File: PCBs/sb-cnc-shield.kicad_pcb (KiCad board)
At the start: 2 copper layers, 68.6 x 53.3 mm, 62 parts, among them P1 XMOT, P2 YMOT, P3 ZMOT, P4 AMOT, P5 UART, P6 I2C, P7 E-STOP, P8 12V-36V, SW1 RESET, U1 ARDUINO_UNO_SHIELD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

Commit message: modify name PCBs
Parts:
- P7: value E-STOP -> ES_SETUP

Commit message: add _SDC_ _SCL_ for hi five rev b board
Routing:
- net SPIN_DIR: track 142.8 -> 144.5 mm

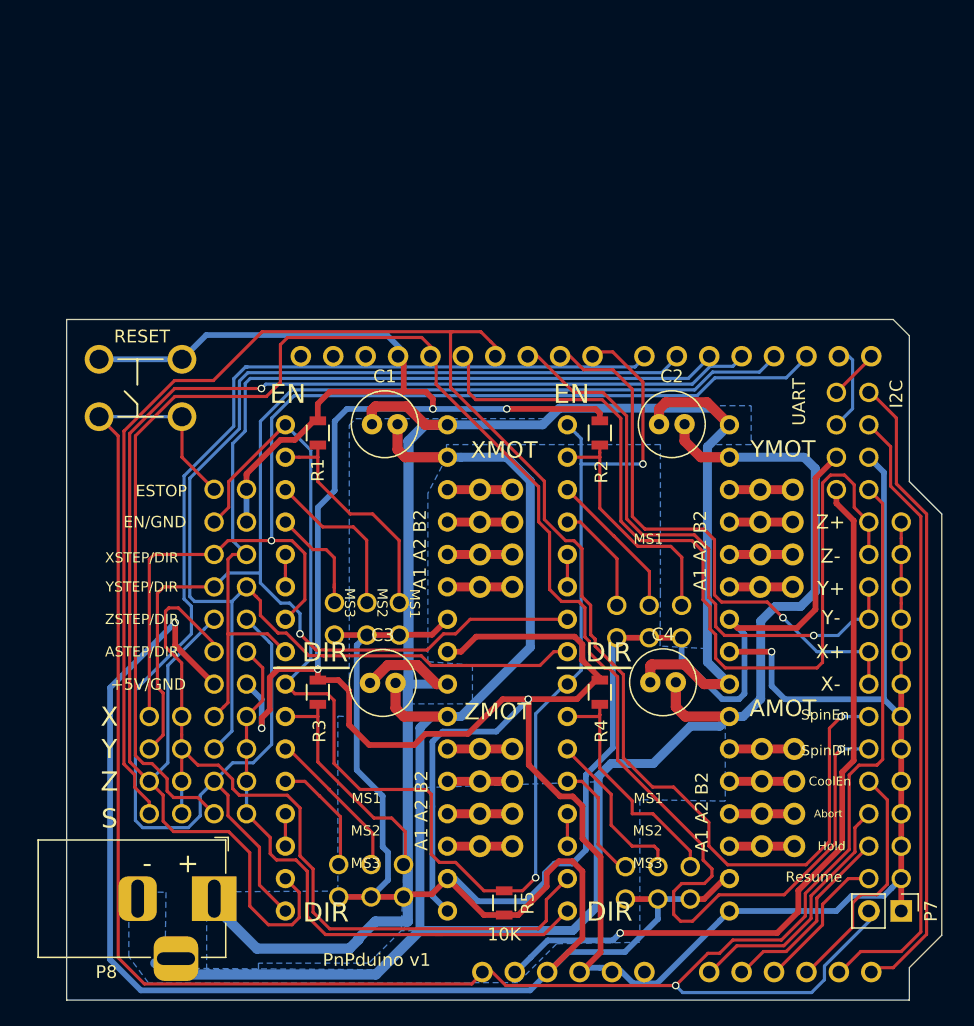
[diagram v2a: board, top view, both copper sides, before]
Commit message: add power button, lenghten pcb
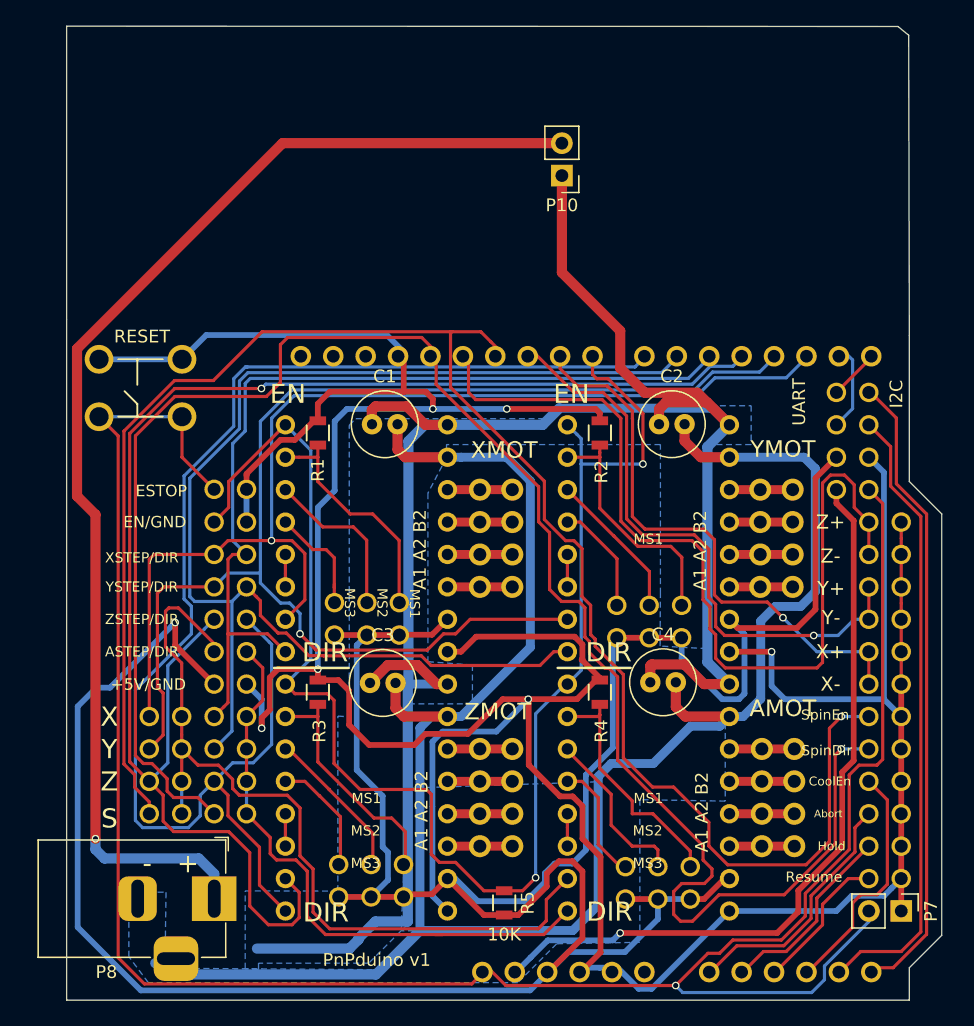
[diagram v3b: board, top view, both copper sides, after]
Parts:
- added P10: power switch, Connector_PinHeader_2.54mm:PinHeader_1x02_P2.54mm_Vertical, F.Cu at (153.1, 54.8)
- P7: value ES_SETUP -> E_STOP
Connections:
- P8 pad 1: VIN -> VIN_
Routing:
- net VIN_: track 0.00 -> 96.6 mm, vias 0 -> 1
- net VIN: track 139.2 -> 161.5 mm
- net +5V: track 226.4 -> 229.1 mm
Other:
- board size 68.6 x 53.3 mm -> 68.6 x 76.3 mm

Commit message: add pump management circuit, I2C JST conn for display, JST power switch
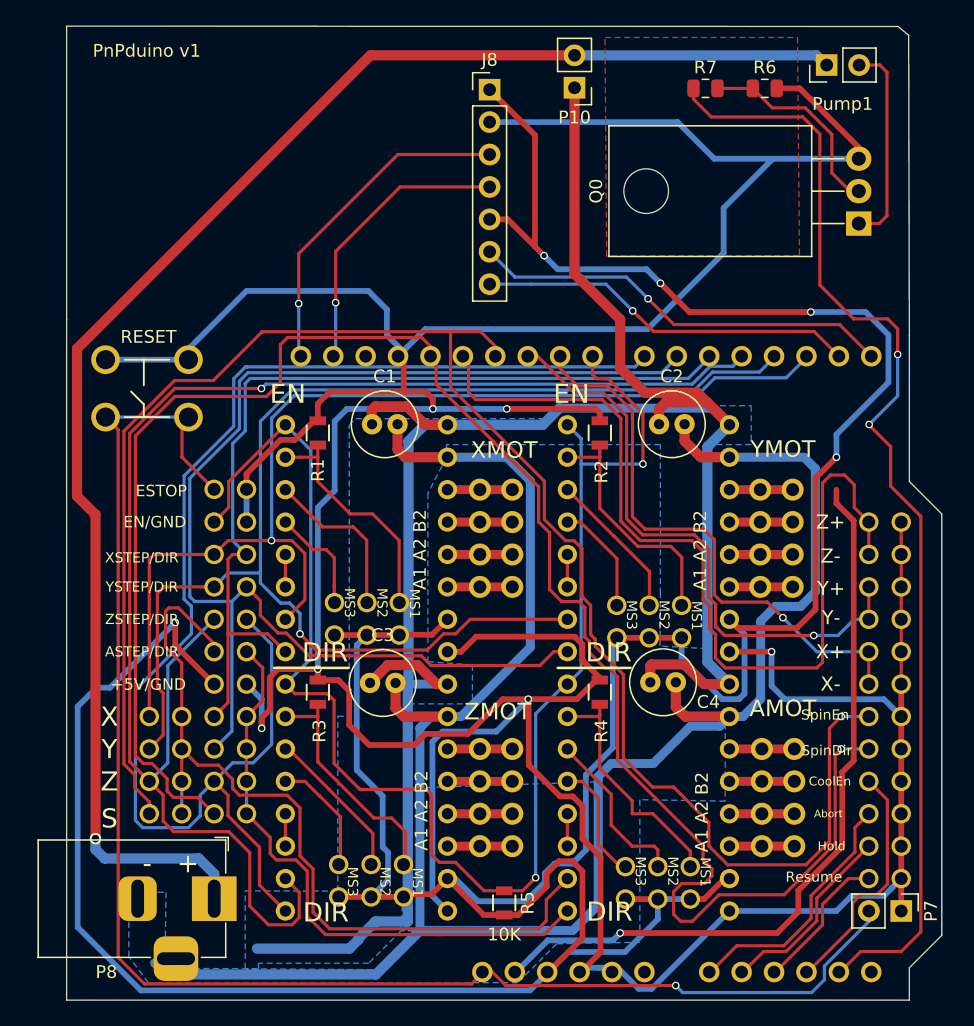
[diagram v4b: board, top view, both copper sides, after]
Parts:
- removed P5: UART, Pin_Headers:Pin_Header_Straight_1x04
- removed P6: I2C, Pin_Headers:Pin_Header_Straight_1x04
- added J8: display, Connector_PinHeader_2.54mm:PinHeader_1x07_P2.54mm_Vertical, F.Cu at (147.4, 48.0)
- added Pump1: pump, Connector_PinHeader_2.54mm:PinHeader_1x02_P2.54mm_Vertical, F.Cu at (173.9, 46.1)
- added Q0: IRF630, Package_TO_SOT_THT:TO-220-3_Horizontal_TabDown, F.Cu at (176.4, 58.5)
- added R6: 10K, Resistor_SMD:R_0805_2012Metric, F.Cu at (169.0, 47.9)
- added R7: 1K, Resistor_SMD:R_0805_2012Metric, F.Cu at (164.4, 47.9)
- moved P10 6.95 mm to (154.1, 47.9)
- moved SW1 0.51 mm to (117.3, 73.7)
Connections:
- U1 pad 1: RX -> DC
- U1 pad 2: TX -> res
- U1 pad 29: Net-(U1-Pad29) -> _SDA_
- U1 pad 30: Net-(U1-Pad30) -> _SCL_
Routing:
- net GND: track 292.6 -> 354.4 mm
- net +5V: track 229.1 -> 289.1 mm, vias 1 -> 5
- net RESET: track 171.4 -> 121.7 mm
- net SCL: track 49.4 -> 0.00 mm
- net SDA: track 48.6 -> 88.3 mm, vias 0 -> 2
- net DC: track 0.00 -> 33.3 mm, vias 0 -> 1
- net res: track 0.00 -> 29.8 mm, vias 0 -> 1
- net _SCL_: track 0.00 -> 26.3 mm, vias 0 -> 1
- net VIN_: track 96.6 -> 120.5 mm
- net _SDA_: track 0.00 -> 22.5 mm, vias 0 -> 1
- net Net-(Q0-Pad2): track 0.00 -> 16.2 mm
- net Net-(Pump1-Pad2): track 0.00 -> 16.1 mm
- net TX: track 6.66 -> 0.00 mm
- net VIN: track 161.5 -> 168.0 mm
- net RX: track 4.49 -> 0.00 mm
- added copper zone on F.Cu, net (none)

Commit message: add voltage regulator shield for 5V rpi
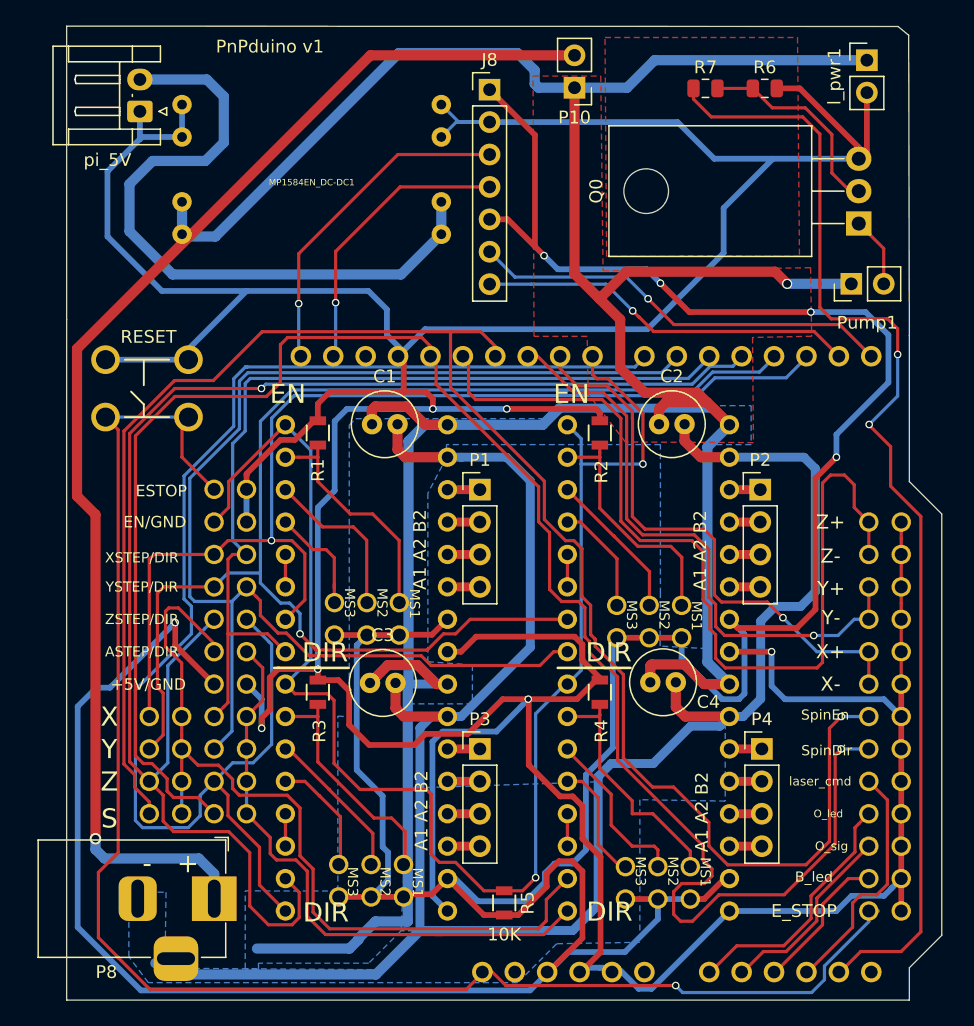
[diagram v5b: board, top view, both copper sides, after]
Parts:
- added MP1584EN_DC-DC1: Conn_01x08, pnp_box:MP1584EN convertisseur DC-DC, F.Cu at (133.5, 54.3)
- added l_pwr1: Conn_01x02, Connector_PinHeader_2.54mm:PinHeader_1x02_P2.54mm_Vertical, F.Cu at (177.0, 45.7)
- added pi_5V: Conn_01x02, Connector_JST:JST_EH_S2B-EH_1x02_P2.50mm_Horizontal, F.Cu at (120.0, 49.7)
- JP21: value CoolEn -> laser_cmd
- JP22: value Abort -> O_led
- JP23: value Hold -> O_sig
- JP24: value Resume -> B_led
- P1, P2, P3, P4: footprint Pin_Headers:Pin_Header_Straight_2x04 -> Connector_PinHeader_2.54mm:PinHeader_1x04_P2.54mm_Vertical
- P7: footprint Connector_PinHeader_2.54mm:PinHeader_1x02_P2.54mm_Vertical -> pnp_box:Pin_100mil_Header_Straight_1x02
- U1: value ARDUINO_UNO_SHIELD -> ARDUINO_UNO_SHIELD/hi five revb
- moved Pump1 17.3 mm to (175.8, 63.2)
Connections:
- net ABORT renamed O_led
- net COOLANT renamed laser_cmd
- net HOLD renamed O_sig
- net Net-(Pump1-Pad2) renamed /D
- net Net-(Q0-Pad2) renamed /G
- net RESUME renamed B_led
- Pump1 pad 1: VIN_ -> VIN
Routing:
- net VIN: track 168.0 -> 253.9 mm, vias 0 -> 1
- net +3V3: track 59.0 -> 0.00 mm, vias 1 -> 0
- net 5V_pi: track 0.00 -> 52.9 mm
- net GND: track 354.4 -> 397.9 mm
- net VIN_: track 120.5 -> 100.4 mm
- net /D: track 16.1 -> 5.53 mm
- net Net-(P4-Pad4): track 5.08 -> 2.54 mm
- net Net-(P4-Pad3): track 5.08 -> 2.54 mm
- net Net-(P4-Pad2): track 5.08 -> 2.54 mm
- net Net-(P4-Pad1): track 5.08 -> 2.54 mm
- net Net-(P3-Pad4): track 5.08 -> 2.54 mm
- net Net-(P3-Pad3): track 5.08 -> 2.54 mm
- net Net-(P3-Pad2): track 5.08 -> 2.54 mm
- net Net-(P3-Pad1): track 5.08 -> 2.54 mm
- net Net-(P2-Pad4): track 4.95 -> 2.41 mm
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- added copper zone on F.Cu, net VIN
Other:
- net class 5V_pi added: clearance 0.2, trace_width 0.8, via_dia 0.6, via_drill 0.4

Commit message: modify kicad and create gerbers then ordering PCBs on JLPCB
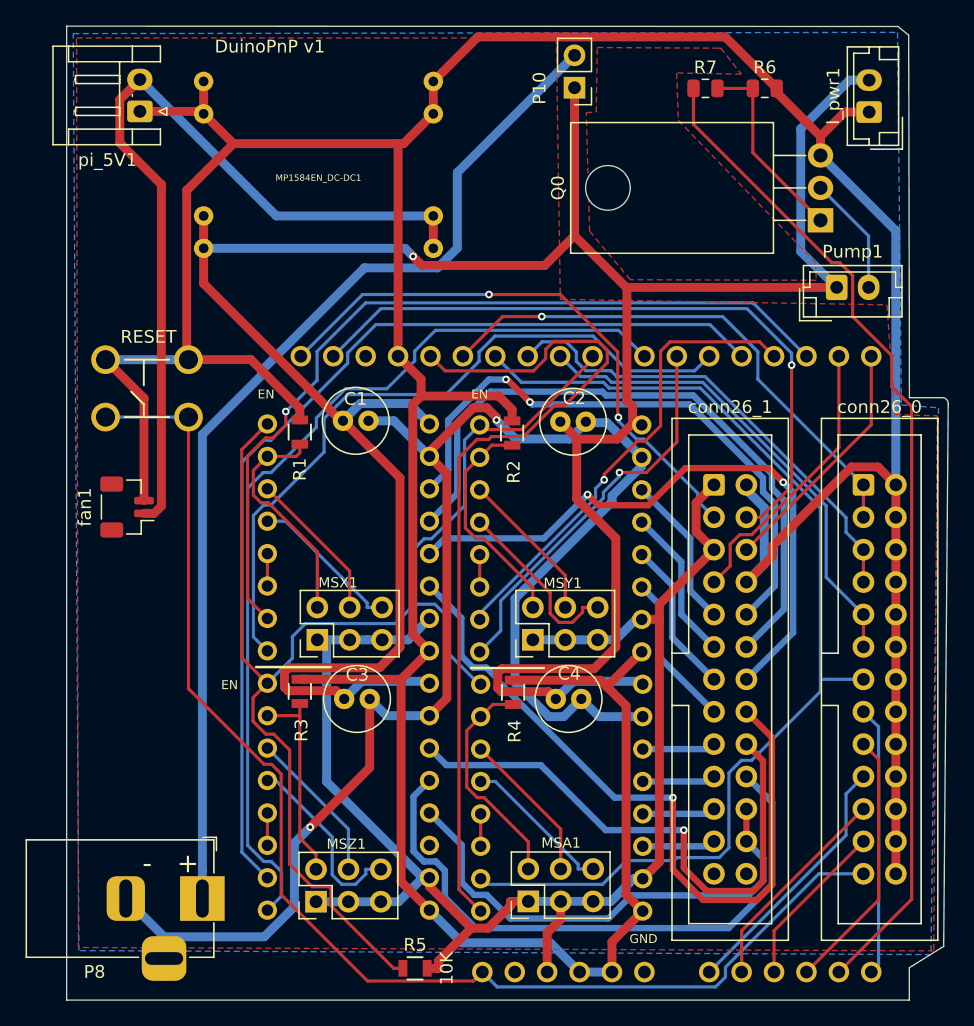
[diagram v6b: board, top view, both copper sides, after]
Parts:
- removed J8: display, Connector_PinHeader_2.54mm:PinHeader_1x07_P2.54mm_Vertical
- removed JP1, JP10, JP11, JP12, JP2, JP3, JP32, JP33, JP34, JP35, JP36, JP37, JP38, JP39, JP4, JP5, JP6, JP7, JP8, JP9: Jumper_NO_Small, footprints:Pin_100mil_Header_Straight_1x02
- removed JP13: Z+, footprints:Pin_100mil_Header_Straight_1x02
- removed JP14: Z-, footprints:Pin_100mil_Header_Straight_1x02
- removed JP15: Y+, footprints:Pin_100mil_Header_Straight_1x02
- removed JP16: Y-, footprints:Pin_100mil_Header_Straight_1x02
- removed JP17: X+, footprints:Pin_100mil_Header_Straight_1x02
- removed JP18: X-, footprints:Pin_100mil_Header_Straight_1x02
- removed JP19: SpinEn, footprints:Pin_100mil_Header_Straight_1x02
- removed JP20: SpinDir, footprints:Pin_100mil_Header_Straight_1x02
- removed JP21: laser_cmd, footprints:Pin_100mil_Header_Straight_1x02
- removed JP22: O_led, footprints:Pin_100mil_Header_Straight_1x02
- removed JP23: O_sig, footprints:Pin_100mil_Header_Straight_1x02
- removed JP24: B_led, footprints:Pin_100mil_Header_Straight_1x02
- removed JP25: ESTOP, footprints:Pin_100mil_Header_Straight_1x02
- removed JP26: EN/GND, footprints:Pin_100mil_Header_Straight_1x02
- removed JP27: XSTEP/DIR, footprints:Pin_100mil_Header_Straight_1x02
- removed JP28: YSTEP/DIR, footprints:Pin_100mil_Header_Straight_1x02
- removed JP29: ZSTEP/DIR, footprints:Pin_100mil_Header_Straight_1x02
- removed JP30: ASTEP/DIR, footprints:Pin_100mil_Header_Straight_1x02
- removed JP31: +5V/GND, footprints:Pin_100mil_Header_Straight_1x02
- removed P1: XMOT, Connector_PinHeader_2.54mm:PinHeader_1x04_P2.54mm_Vertical
- removed P2: YMOT, Connector_PinHeader_2.54mm:PinHeader_1x04_P2.54mm_Vertical
- removed P3: ZMOT, Connector_PinHeader_2.54mm:PinHeader_1x04_P2.54mm_Vertical
- removed P4: AMOT, Connector_PinHeader_2.54mm:PinHeader_1x04_P2.54mm_Vertical
- removed P7: E_STOP, pnp_box:Pin_100mil_Header_Straight_1x02
- added MSA1: MSA, Connector_PinHeader_2.54mm:PinHeader_2x03_P2.54mm_Vertical, F.Cu at (150.5, 111.6)
- added MSX1: MSX, Connector_PinHeader_2.54mm:PinHeader_2x03_P2.54mm_Vertical, F.Cu at (133.9, 91.1)
- added MSY1: MSY, Connector_PinHeader_2.54mm:PinHeader_2x03_P2.54mm_Vertical, F.Cu at (150.8, 91.1)
- added MSZ1: MSZ, Connector_PinHeader_2.54mm:PinHeader_2x03_P2.54mm_Vertical, F.Cu at (133.8, 111.7)
- added conn26_0: 0, Connector_IDC:IDC-Header_2x13_P2.54mm_Vertical, F.Cu at (176.7, 79.0)
- added conn26_1: 1, Connector_IDC:IDC-Header_2x13_P2.54mm_Vertical, F.Cu at (165.0, 79.0)
- added fan1: fan5V, Connector_JST:JST_SH_BM02B-SRSS-TB_1x02-1MP_P1.00mm_Vertical, F.Cu at (119.0, 80.7)
- Pump1, l_pwr1: footprint Connector_PinHeader_2.54mm:PinHeader_1x02_P2.54mm_Vertical -> Connector_JST:JST_EH_B2B-EH-A_1x02_P2.50mm_Vertical
- moved R5 8.67 mm to (141.6, 116.9), turned to 180 degrees
- moved C2 7.74 mm to (153.0, 74.1)
- moved C4 7.52 mm to (152.6, 95.8)
- moved U3 6.87 mm to (146.7, 74.3)
- moved R2 6.87 mm to (149.2, 74.9)
- moved R4 6.80 mm to (149.3, 95.3)
- moved U5 6.80 mm to (146.7, 94.6)
- moved l_pwr1 4.07 mm to (177.2, 49.8), turned to 90 degrees
- moved Q0 3.01 mm to (173.4, 58.3)
- moved C3 2.38 mm to (136.1, 95.8)
- moved C1 2.29 mm to (136.0, 74.0)
- moved R1 1.41 mm to (132.6, 74.9)
- moved R3 1.41 mm to (132.6, 95.2)
- moved U2 1.41 mm to (130.0, 74.2)
- moved U4 1.41 mm to (130.0, 94.5)
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- renumbered pi_5V to pi_5V1
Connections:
- net SDA renamed pump_ctrl
- U1 pad 17: SCL -> B_sig
- U1 pad 19: laser_cmd -> up_light
- U2 pad 11: Net-(P1-Pad4) -> x1B
- U2 pad 12: Net-(P1-Pad3) -> x1A
- U2 pad 13: Net-(P1-Pad2) -> x2A
- U2 pad 14: Net-(P1-Pad1) -> x2B
- U3 pad 11: Net-(P2-Pad4) -> y1B
- U3 pad 12: Net-(P2-Pad3) -> y1A
- U3 pad 13: Net-(P2-Pad2) -> y2A
- U3 pad 14: Net-(P2-Pad1) -> y2B
- U4 pad 11: Net-(P3-Pad4) -> z1B
- U4 pad 12: Net-(P3-Pad3) -> z1A
- U4 pad 13: Net-(P3-Pad2) -> z2A
- U4 pad 14: Net-(P3-Pad1) -> z2B
- U5 pad 11: Net-(P4-Pad4) -> a1B
- U5 pad 12: Net-(P4-Pad3) -> a1A
- U5 pad 13: Net-(P4-Pad2) -> a2A
- U5 pad 14: Net-(P4-Pad1) -> a2B
- U5 pad 7: ASTEP -> SPIN_EN
- U5 pad 8: ADIR -> SPIN_DIR
- l_pwr1 pad 1: VIN -> GND
- l_pwr1 pad 2: GND -> VIN
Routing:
- net +5V: track 289.1 -> 117.5 mm, vias 5 -> 0
- net SPIN_DIR: track 144.5 -> 67.9 mm, vias 1 -> 0
- net YDIR: track 100.2 -> 30.8 mm, vias 0 -> 1
- net YSTEP: track 105.4 -> 36.9 mm
- net ASTEP: track 65.6 -> 0.00 mm
- net GND: track 397.9 -> 336.0 mm, vias 6 -> 0
- net x1B: track 0.00 -> 57.1 mm, vias 0 -> 1
- net SPIN_EN: track 137.6 -> 84.7 mm, vias 1 -> 0
- net x2A: track 0.00 -> 52.0 mm
- net x1A: track 0.00 -> 48.9 mm, vias 0 -> 2
- net z2A: track 0.00 -> 48.6 mm
- net x2B: track 0.00 -> 47.2 mm, vias 0 -> 2
- net ADIR: track 46.9 -> 0.00 mm
- net z2B: track 0.00 -> 44.1 mm, vias 0 -> 1
- net ZSTEP: track 117.5 -> 78.5 mm, vias 1 -> 0
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- added copper zone on B.Cu, net GND
- removed copper zone on B.Cu, net GNDA
- removed copper zone on B.Cu, net VIN
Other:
- board size 68.6 x 76.3 mm -> 69.1 x 76.3 mm
- net class 5V: trace_width 0.45 -> 0.7
- net class 5V_pi: trace_width 0.8 -> 0.7
- net class GND added: clearance 0.2, trace_width 0.7, via_dia 0.6, via_drill 0.4
- net class mot added: clearance 0.2, trace_width 0.5, via_dia 0.6, via_drill 0.4
- board text added: "DuinoPnP v1"
- board text added: "GND"
- board text removed: "A1 A2 B2"
- board text removed: "DIR"
- board text removed: "MS1"
- board text removed: "MS2"
- board text removed: "MS3"
- board text removed: "PnPduino v1"
- board text removed: "S"
- board text removed: "X"
- board text removed: "Y"
- board text removed: "Z"
